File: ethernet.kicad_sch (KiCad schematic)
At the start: 36 parts

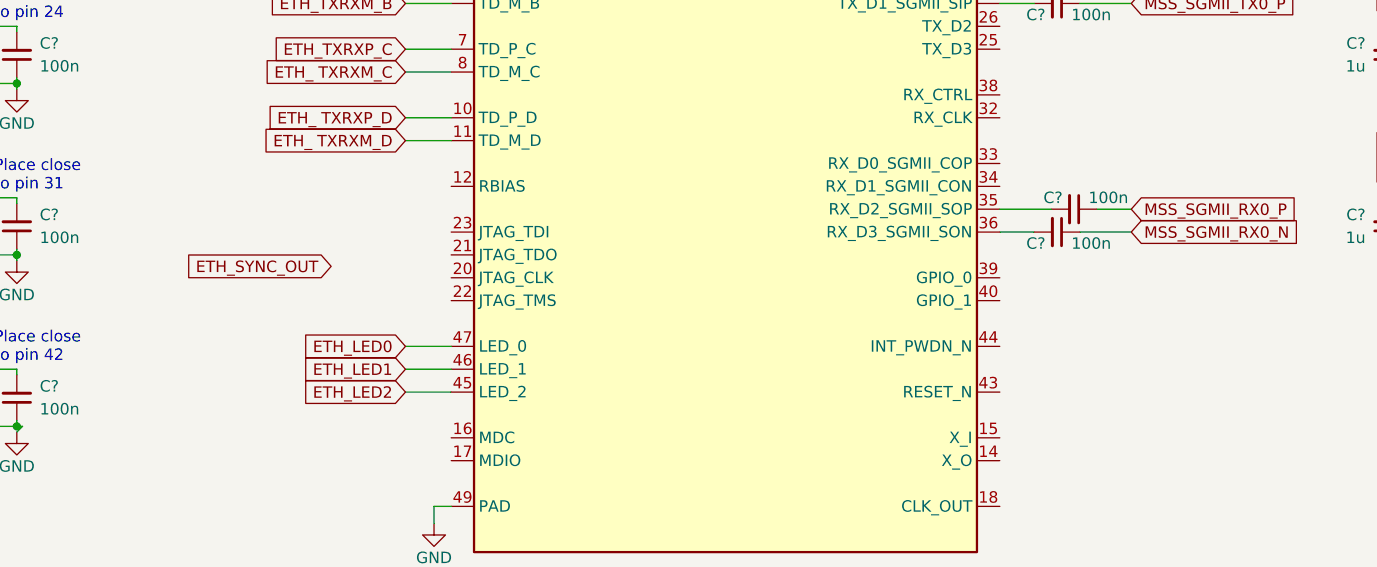
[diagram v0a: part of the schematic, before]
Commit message: [#53847] Reconnect ETH sync pins to DP83867ISRGZR GPIOs
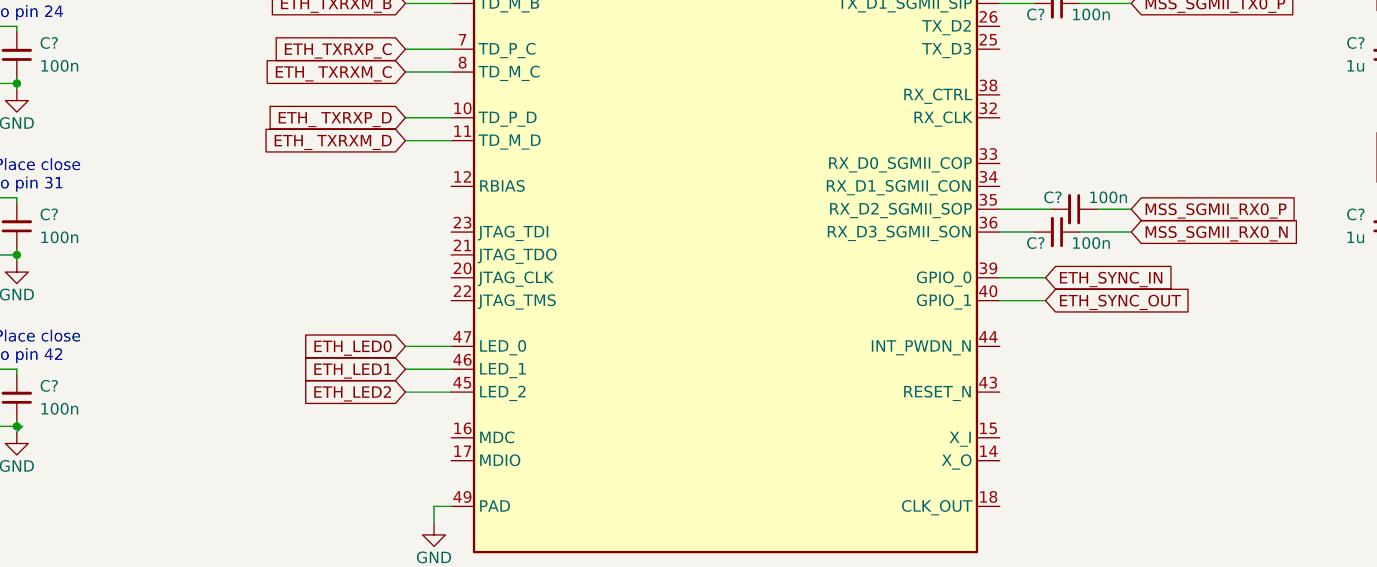
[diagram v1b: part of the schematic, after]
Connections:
- net ETH_SYNC_OUT: now also U?.40 (GPIO_1)
- net ETH_SYNC_IN: now reaches U?.39 (GPIO_0)
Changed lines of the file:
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@@
+    (stroke (width 0) (type default) (color 0 0 0 0))
+  )
+  (wire (pts (xy 242.57 129.54) (xy 247.65 129.54))
     (stroke (width 0) (type default) (color 0 0 0 0))
   )
@@
   )
   (wire (pts (xy 311.15 107.95) (xy 317.5 107.95))
+    (stroke (width 0) (type default) (color 0 0 0 0))
+  )
+  (wire (pts (xy 242.57 132.08) (xy 247.65 132.08))
     (stroke (width 0) (type default) (color 0 0 0 0))
   )
@@
     )
   )
-  (global_label "ETH_SYNC_OUT" (shape input) (at 168.275 128.27 180) (fields_autoplaced)
-    (effects (font (size 1.27 1.27)) (justify right))
-    (property "Intersheet References" "${INTERSHEET_REFS}" (id 0) (at 151.9524 128.1906 0)
-      (effects (font (size 1.27 1.27)) (justify right) hide)
+  (global_label "ETH_SYNC_OUT" (shape input) (at 247.65 132.08 0) (fields_autoplaced)
+    (effects (font (size 1.27 1.27)) (justify left))
+    (property "Intersheet References" "${INTERSHEET_REFS}" (id 0) (at 263.9726 132.0006 0)
+      (effects (font (size 1.27 1.27)) (justify left) hide)
     )
   )
@@
     )
   )
+  (global_label "ETH_SYNC_IN" (shape input) (at 247.65 129.54 0) (fields_autoplaced)
+    (effects (font (size 1.27 1.27)) (justify left))
+    (property "Intersheet References" "${INTERSHEET_REFS}" (id 0) (at 262.2793 129.4606 0)
+      (effects (font (size 1.27 1.27)) (justify left) hide)
+    )
+  )

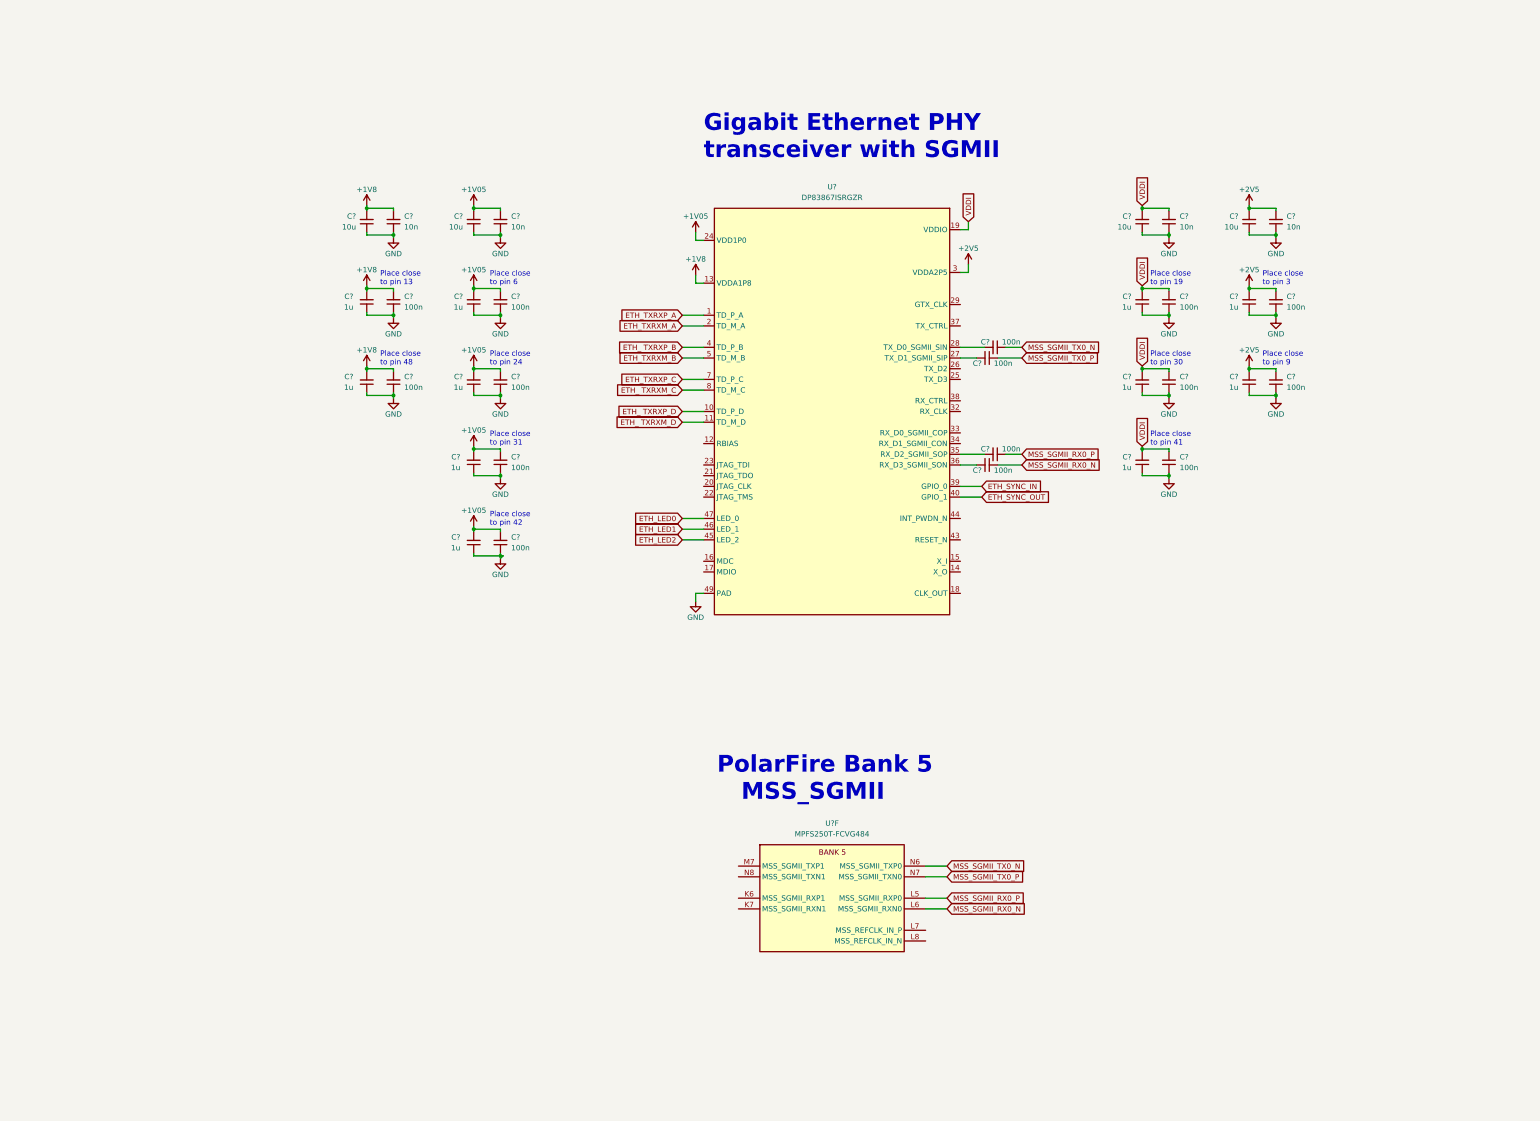
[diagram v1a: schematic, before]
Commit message: [#54016] Place components to assess available space
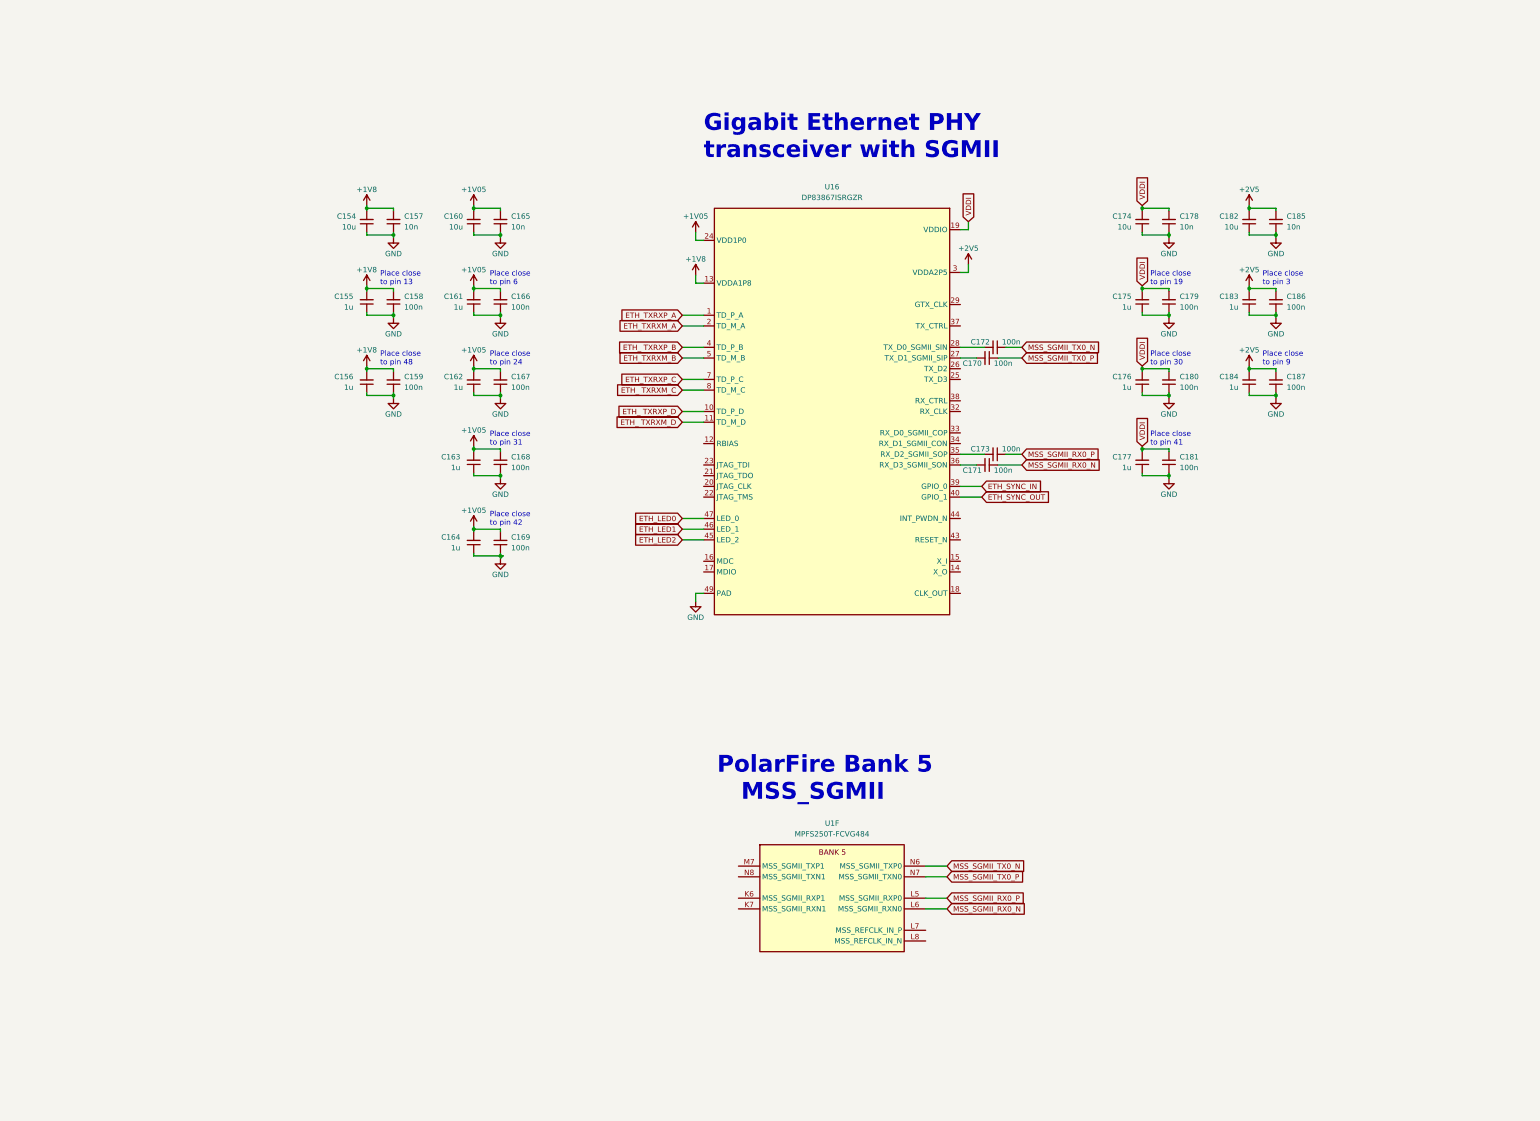
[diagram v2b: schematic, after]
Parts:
- gave numbers to parts that had none: 36

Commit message: [#54442] Add crystal to ethernet transceiver
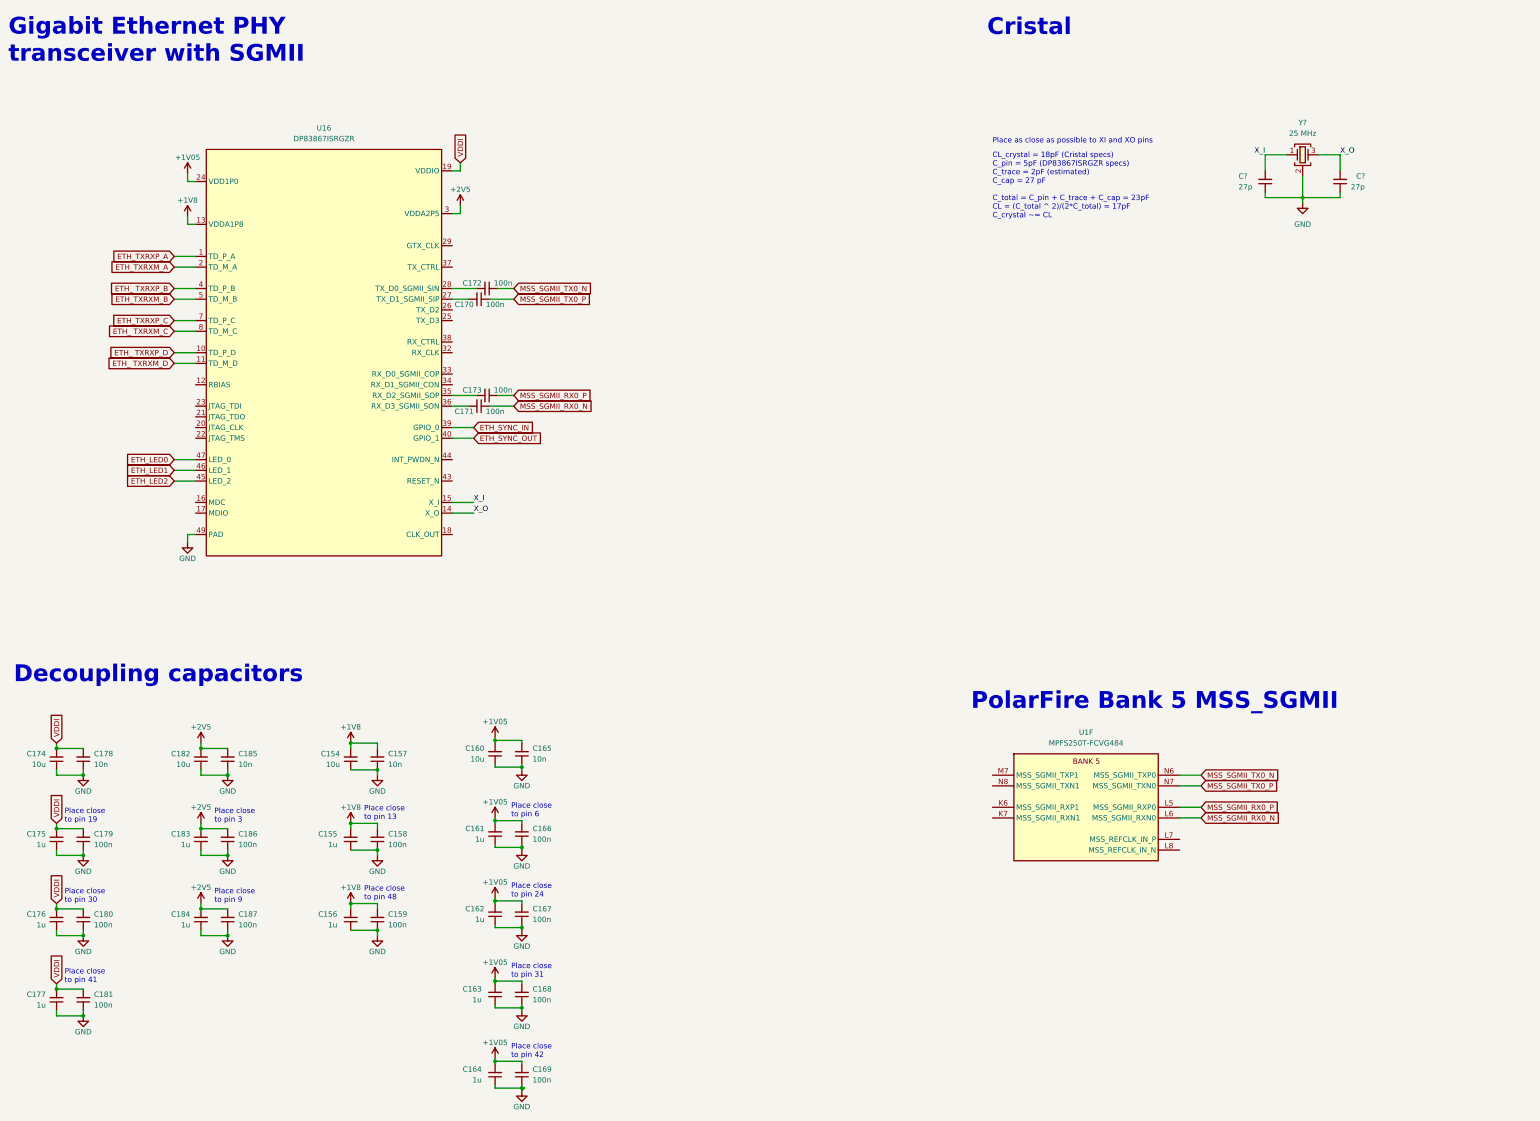
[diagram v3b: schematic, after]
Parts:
- added C? (x2): C_27p_0402, antmicro-footprints:C_0402_1005Metric, symbol antmicroCapacitors0402:C_27p_0402
- added Y?: Resonator_25MHz_ABM8G, antmicro-footprints:Oscillator_SMD_Geyer_KX-7-4Pin_3.2x2.5mm, symbol antmicroResonators:Resonator_25MHz_ABM8G
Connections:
- net GND: now also C?.1, C?.1, Y?.2 (SH), Y?.4 (SH)
- net X_O: now reaches U16.14 (X_O)
- net X_O: now also C?.2, Y?.3
- net X_I: now reaches U16.15 (X_I)
- net X_I: now also C?.2, Y?.1
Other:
- note added: "CL_crystal = 18pF (Cristal specs) C_pin = 5pF (DP83867ISRGZR specs) C_trace = 2pF (estimated) C_cap = 27 pF C_total = C_pin + C_trace + C_cap = 23pF CL = (C_total ^ 2)/(2*C_total) = 17pF C_crystal ~= CL"
- note added: "Cristal"
- note added: "Decoupling capacitors"
- note added: "Place as close as possible to XI and XO pins"
- moved on the sheet: C154, C155, C156, C157, C158, C159, C160, C161, C162, C163, C164, C165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
